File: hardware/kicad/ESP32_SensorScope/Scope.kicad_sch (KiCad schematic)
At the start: 4 parts, among them U16 74LVC1G240DBVRG4

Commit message: Various changes
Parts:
- removed C25: 100n, symbol Device:C
- removed D12: LED_RX, symbol Device:LED
- removed R45: 510, symbol Device:R
- removed U16: 74LVC1G240DBVRG4, Package_TO_SOT_SMD:SOT-23-5, symbol SN74LVC1G240:74LVC1G240DBVRG4
- added R10, R7, R8, R9: R, symbol Device:R
- added U12: OPA333xxDBV, Package_TO_SOT_SMD:SOT-23-5, symbol Amplifier_Operational:OPA333xxDBV
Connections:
- net GND: now also R9.2, U12.2 (V-)
- new net: R10.1, R7.2, U12.4 (-)
- new net: R10.2, U12.1
- new net: R8.2, R9.1, U12.3 (+)
- new net V_ref: R8.1

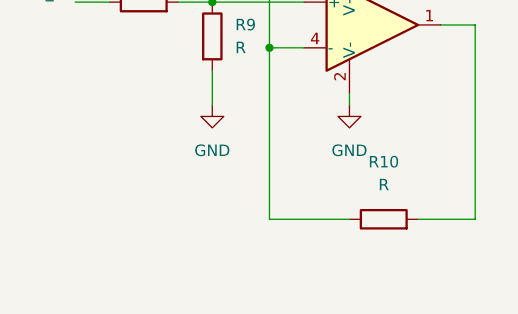
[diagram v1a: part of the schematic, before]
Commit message: Adde LCD Part
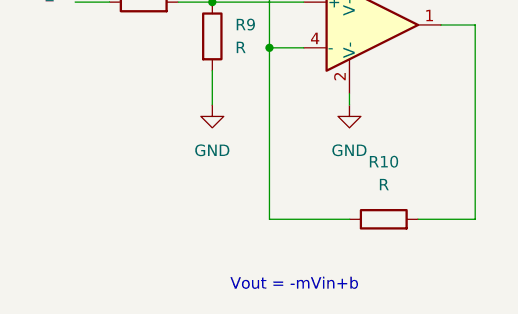
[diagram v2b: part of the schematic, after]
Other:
- note added: "Vout = -mVin+b"

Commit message: updated scope
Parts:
- removed R8, R9: R, symbol Device:R
- added C30: C, symbol Device:C
- added C31: 100n, symbol Device:C
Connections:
- net +3.3V: now also U12.5 (V+), C31.1
- net GND: now also C31.2
- net V_ref: now also U12.3 (+)
- net at R10.1, R7.2, U12.4 (-): now also C30.2
- net To ADC: now reaches R10.2, U12.1
- net To ADC: now also C30.1
- net Ain: now reaches R7.1
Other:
- note added: "Lowpass filter"
- note added: "V_ref adjusts the offset voltage Adjust to measure negative voltages"
- moved on the sheet: R10, R7

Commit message: something probobly
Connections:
- net To ADC renamed Ch1_ADC
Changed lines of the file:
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@@
 	(wire
 		(pts
-			(xy 128.27 93.98) (xy 135.89 93.98)
+			(xy 133.35 93.98) (xy 128.27 93.98)
 		)
 		(stroke
@@
 		)
 	)
-	(label "To ADC"
-		(at 135.89 93.98 0)
-		(fields_autoplaced yes)
-		(effects
-			(font
-				(size 1.27 1.27)
-			)
-			(justify left bottom)
-		)
-	)
 	(label "Ain"
 		(at 81.28 93.98 180)
@@
 		)
 	)
+	(global_label "Ch2_ADC"
+		(shape input)
+		(at 140.97 80.01 0)
+		(fields_autoplaced yes)
+		(effects
+			(font
+				(size 1.27 1.27)
+			)
+			(justify left)
+		)
+		(property "Intersheetrefs" "${INTERSHEET_REFS}"
+			(at 152.1799 80.01 0)
+			(effects
+				(font
+					(size 1.27 1.27)
+				)
+				(justify left)
+				(hide yes)
+			)
+		)
+	)
+	(global_label "Ch1_ADC"
+		(shape input)
+		(at 133.35 93.98 0)
+		(fields_autoplaced yes)
+		(effects
+			(font
+				(size 1.27 1.27)
+			)
+			(justify left)
+		)
+		(property "Intersheetrefs" "${INTERSHEET_REFS}"
+			(at 144.5599 93.98 0)
+			(effects
+				(font
+					(size 1.27 1.27)
+				)
+				(justify left)
+				(hide yes)
+			)
+		)
+	)

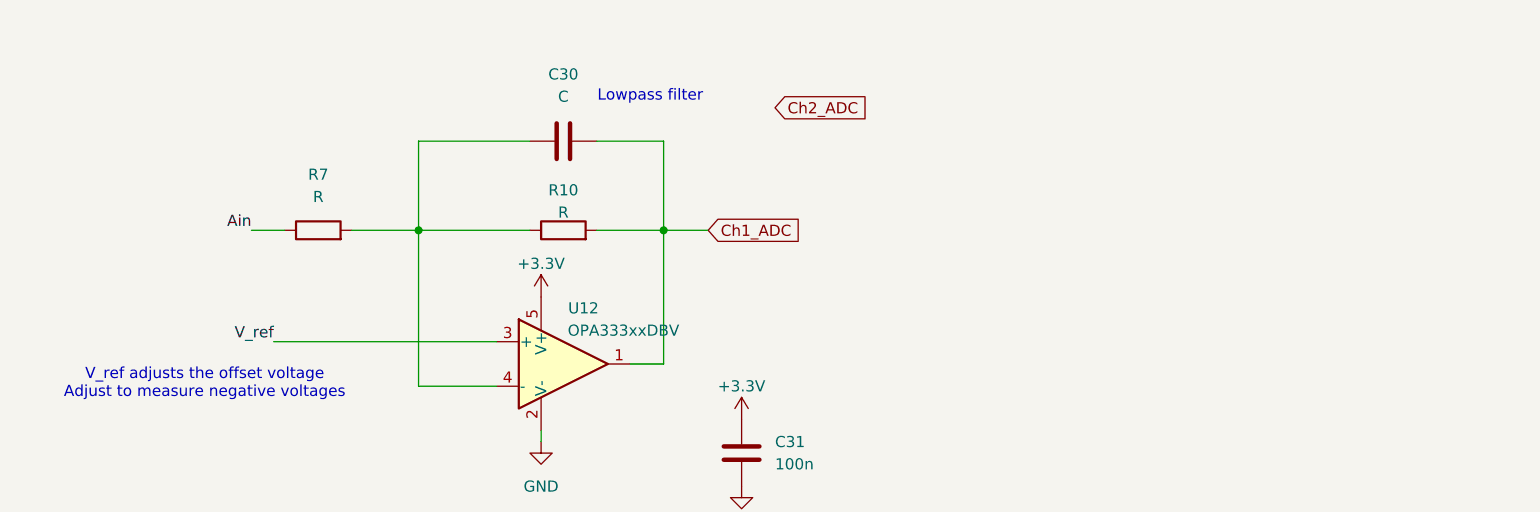
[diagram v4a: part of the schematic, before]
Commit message: som updates on the schematics
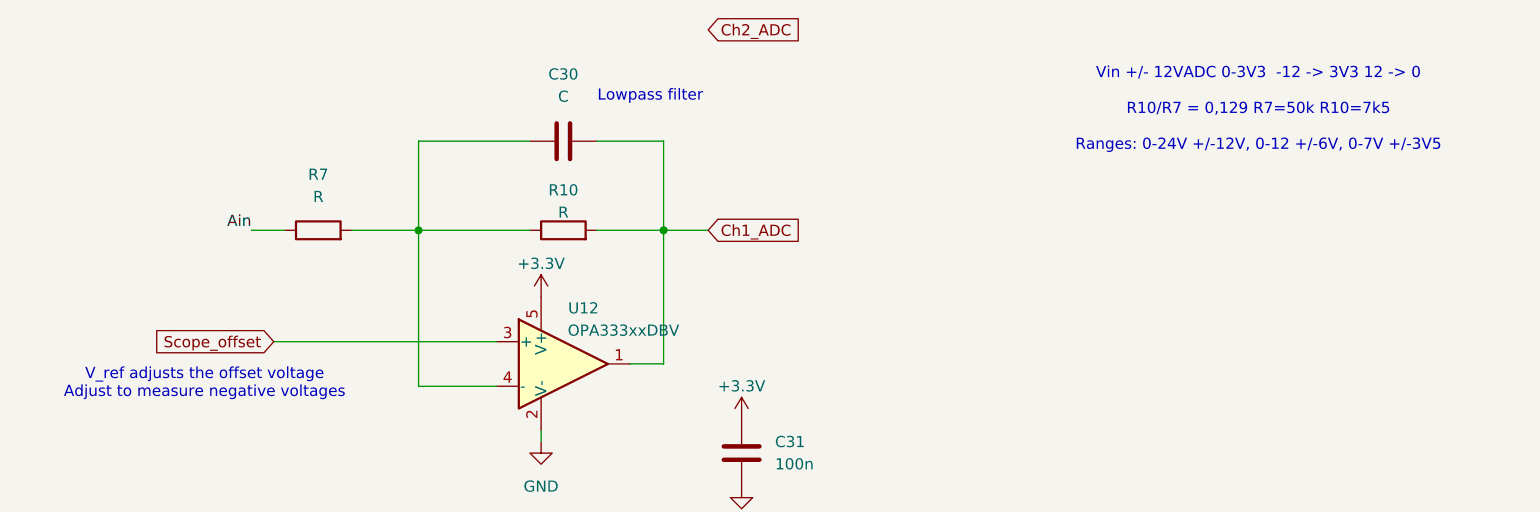
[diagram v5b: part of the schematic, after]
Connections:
- net V_ref renamed Scope_offset
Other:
- note added: "Vin +/- 12VADC 0-3V3 -12 -> 3V3 12 -> 0 R10/R7 = 0,129 R7=50k R10=7k5 Ranges: 0-24V +/-12V, 0-12 +/-6V, 0-7V +/-3V5"
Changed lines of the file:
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@@
+		)
+	)
+	(text "Vin +/- 12VADC 0-3V3  -12 -> 3V3 12 -> 0\n\nR10/R7 = 0,129 R7=50k R10=7k5\n\nRanges: 0-24V +/-12V, 0-12 +/-6V, 0-7V +/-3V5"
+		(exclude_from_sim no)
+		(at 196.088 80.264 0)
+		(effects
+			(font
+				(size 1.27 1.27)
+			)
 		)
 	)
@@
 		)
 	)
-	(label "V_ref"
-		(at 83.82 106.68 180)
-		(fields_autoplaced yes)
-		(effects
-			(font
-				(size 1.27 1.27)
-			)
-			(justify right bottom)
-		)
-	)
 	(global_label "Ch2_ADC"
 		(shape input)
-		(at 140.97 80.01 0)
+		(at 133.35 71.12 0)
 		(fields_autoplaced yes)
 		(effects
@@
 		)
 		(property "Intersheetrefs" "${INTERSHEET_REFS}"
-			(at 152.1799 80.01 0)
+			(at 144.5599 71.12 0)
 			(effects
 				(font
@@
 				)
 				(justify left)
-				(hide yes)
+			)
+		)
+	)
+	(global_label "Scope_offset"
+		(shape input)
+		(at 83.82 106.68 180)
+		(fields_autoplaced yes)
+		(effects
+			(font
+				(size 1.27 1.27)
+			)
+			(justify right)
+		)
+		(property "Intersheetrefs" "${INTERSHEET_REFS}"
+			(at 68.7397 106.68 0)
+			(effects
+				(font
+					(size 1.27 1.27)
+				)
+				(justify right)
 			)
 		)
@@
 				)
 				(justify left)
-				(hide yes)
 			)
 		)

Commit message: updatet schematic
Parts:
- R10: value R -> 7K5
- R7: value R -> 50K
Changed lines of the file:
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@@
 			)
 		)
-		(property "Value" "R"
+		(property "Value" "7K5"
 			(at 116.84 91.948 90)
 			(effects
@@
 			)
 		)
-		(property "Value" "R"
+		(property "Value" "50K"
 			(at 88.9 90.17 90)
 			(effects

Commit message: addet some footprints"
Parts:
- C31: footprint (none) -> Capacitor_SMD:C_0805_2012Metric
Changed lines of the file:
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@@
 			)
 		)
-		(property "Footprint" ""
+		(property "Footprint" "Capacitor_SMD:C_0805_2012Metric"
 			(at 138.1252 123.19 0)
 			(effects
